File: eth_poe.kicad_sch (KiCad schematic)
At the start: 19 parts, among them U4 DP1435-5V

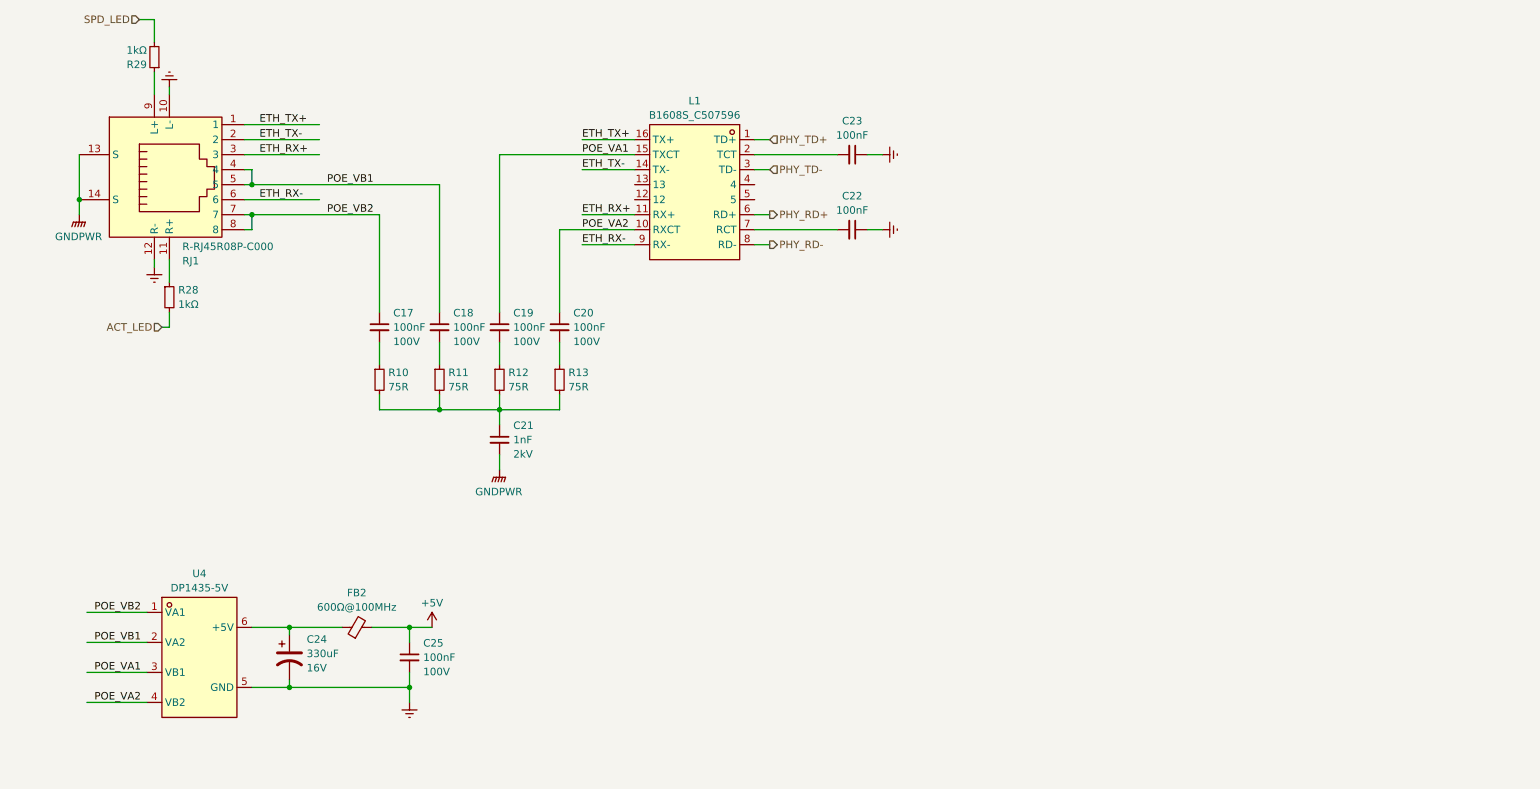
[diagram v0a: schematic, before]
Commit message: Update pcb & sch for T113 SOM
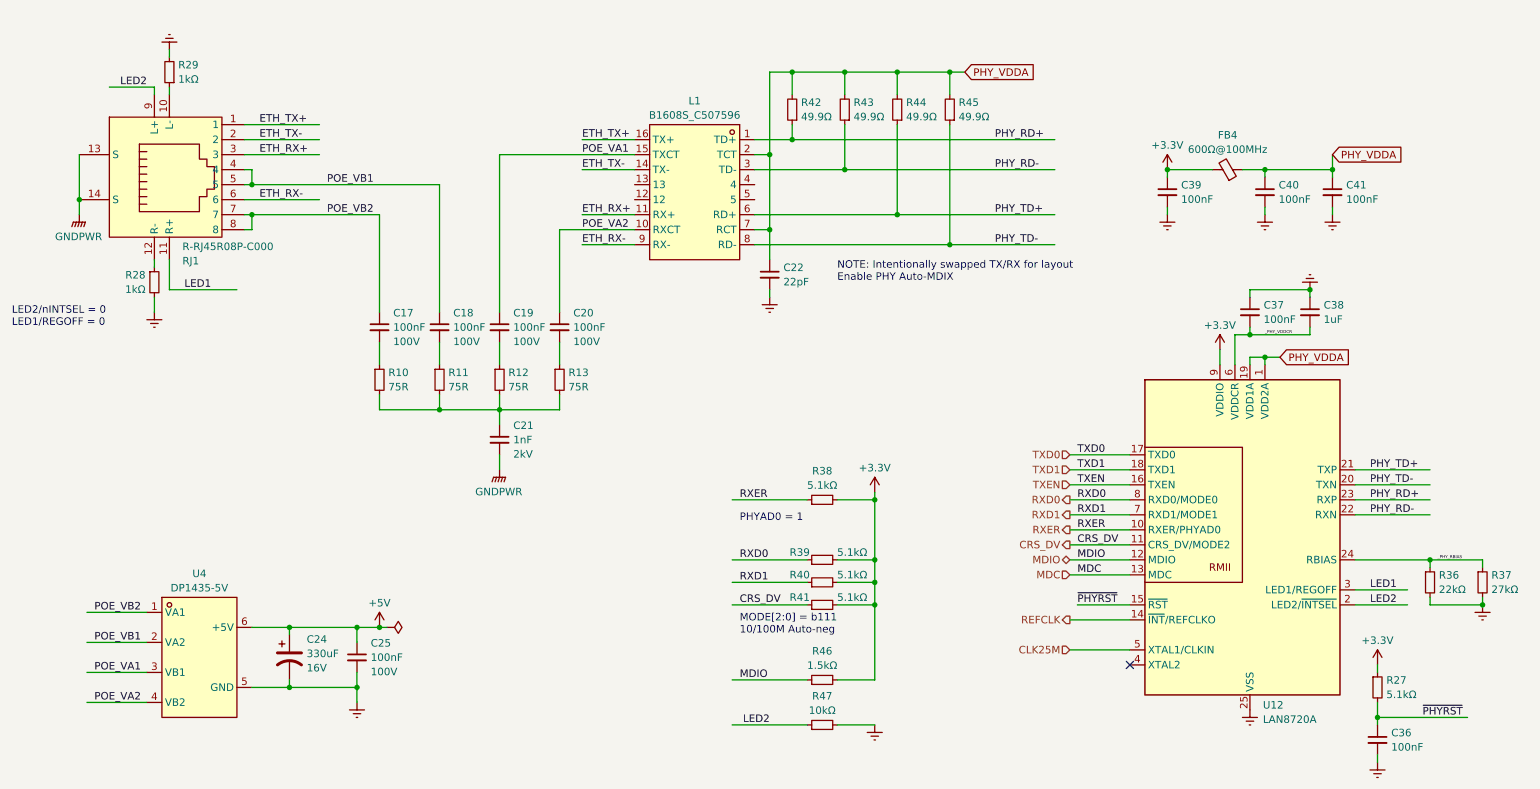
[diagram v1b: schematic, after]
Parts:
- removed C23: 100nF, Capacitor_SMD:C_0402_1005Metric, symbol Device:C_Small
- removed FB2: 600Ω@100MHz, Inductor_SMD:L_0603_1608Metric, symbol Device:FerriteBead_Small
- added C36, C37, C39, C40, C41: 100nF, Capacitor_SMD:C_0402_1005Metric, symbol Device:C_Small
- added C38: 1uF, Capacitor_SMD:C_0402_1005Metric, symbol Device:C_Small
- added FB4: 600Ω@100MHz, Inductor_SMD:L_0603_1608Metric, symbol Device:FerriteBead_Small
- added R27, R38, R39, R40, R41: 5.1kΩ, Resistor_SMD:R_0402_1005Metric, symbol Device:R_Small
- added R36: 22kΩ, Resistor_SMD:R_0402_1005Metric, symbol Device:R_Small
- added R37: 27kΩ, Resistor_SMD:R_0603_1608Metric, symbol Device:R_Small
- added R42, R43, R44, R45: 49.9Ω, Resistor_SMD:R_0402_1005Metric, symbol Device:R_Small
- added R46: 1.5kΩ, Resistor_SMD:R_0402_1005Metric, symbol Device:R_Small
- added R47: 10kΩ, Resistor_SMD:R_0402_1005Metric, symbol Device:R_Small
- added U12: LAN8720A, Package_DFN_QFN:VQFN-24-1EP_4x4mm_P0.5mm_EP2.5x2.5mm, symbol Interface_Ethernet:LAN8720A
- C22: value 100nF -> 22pF
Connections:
- net ACT_LED is gone; now on net Earth: R28.2
- net SPD_LED is gone; now on net Earth: R29.2
- net +5V: now also C24.1, U4.6 (+5V)
- net Earth: now also C22.2, C36.2, C37.1, C38.1, C39.2, C40.2, C41.2, R36.2, R37.2, R47.2, U12.25 (VSS); no longer C22.1, RJ1.10 (L-), RJ1.12 (R-)
- net PHY_RD+: now also L1.1 (TD+), R42.1, U12.23 (RXP); no longer L1.6 (RD+)
- net PHY_RD-: now also L1.3 (TD-), R43.1, U12.22 (RXN); no longer L1.8 (RD-)
- net PHY_TD+: now also L1.6 (RD+), R44.1, U12.21 (TXP); no longer L1.1 (TD+)
- net PHY_TD-: now also L1.8 (RD-), R45.1, U12.20 (TXN); no longer L1.3 (TD-)
- net PHY_VDDA: now reaches L1.7 (RCT)
- net PHY_VDDA: now also C22.1, L1.2 (TCT), C40.1, C41.1, FB4.1, R42.2, R43.2, R44.2, R45.2, U12.1 (VDD2A), U12.19 (VDD1A); no longer C22.2
- net at R28.1: now also RJ1.12 (R-); no longer RJ1.11 (R+)
- net at R29.1: now also RJ1.10 (L-); no longer RJ1.9 (L+)
- new net +3.3V: C39.1, FB4.2, R27.1, R38.2, R39.2, R40.2, R41.2, R46.2, U12.9 (VDDIO)
- new net CLK25M: U12.5 (XTAL1/CLKIN)
- new net CRS_DV: R41.1, U12.11 (CRS_DV/MODE2)
- new net LED1: RJ1.11 (R+), U12.3 (LED1/REGOFF)
- new net LED2: R47.1, RJ1.9 (L+), U12.2 (LED2/~{INTSEL})
- new net MDC: U12.13 (MDC)
- new net MDIO: R46.1, U12.12 (MDIO)
- new net REFCLK: U12.14 (~{INT}/REFCLKO)
- new net RXD0: R39.1, U12.8 (RXD0/MODE0)
- new net RXD1: R40.1, U12.7 (RXD1/MODE1)
- new net RXER: R38.1, U12.10 (RXER/PHYAD0)
- new net TXD0: U12.17 (TXD0)
- new net TXD1: U12.18 (TXD1)
- new net TXEN: U12.16 (TXEN)
- new net _PHY_RBIAS: R36.1, R37.1, U12.24 (RBIAS)
- new net _PHY_VDDCR: C37.2, C38.2, U12.6 (VDDCR)
- new net ~{PHYRST}: C36.1, R27.2, U12.15 (~{RST})
- no-connect marks 0 -> 1
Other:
- note added: "LED2/nINTSEL = 0 LED1/REGOFF = 0"
- note added: "MODE[2:0] = b111 10/100M Auto-neg"
- note added: "NOTE: Intentionally swapped TX/RX for layout Enable PHY Auto-MDIX"
- note added: "PHYAD0 = 1"
- moved on the sheet: C25
